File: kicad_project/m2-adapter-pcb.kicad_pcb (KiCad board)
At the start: 2 copper layers, 100 x 45 mm, 19 parts, among them J1 Bus_M.2_Socket_B, J2 SATA-7P, J3 JST S2B-PH-K-S, U1 TPS563200

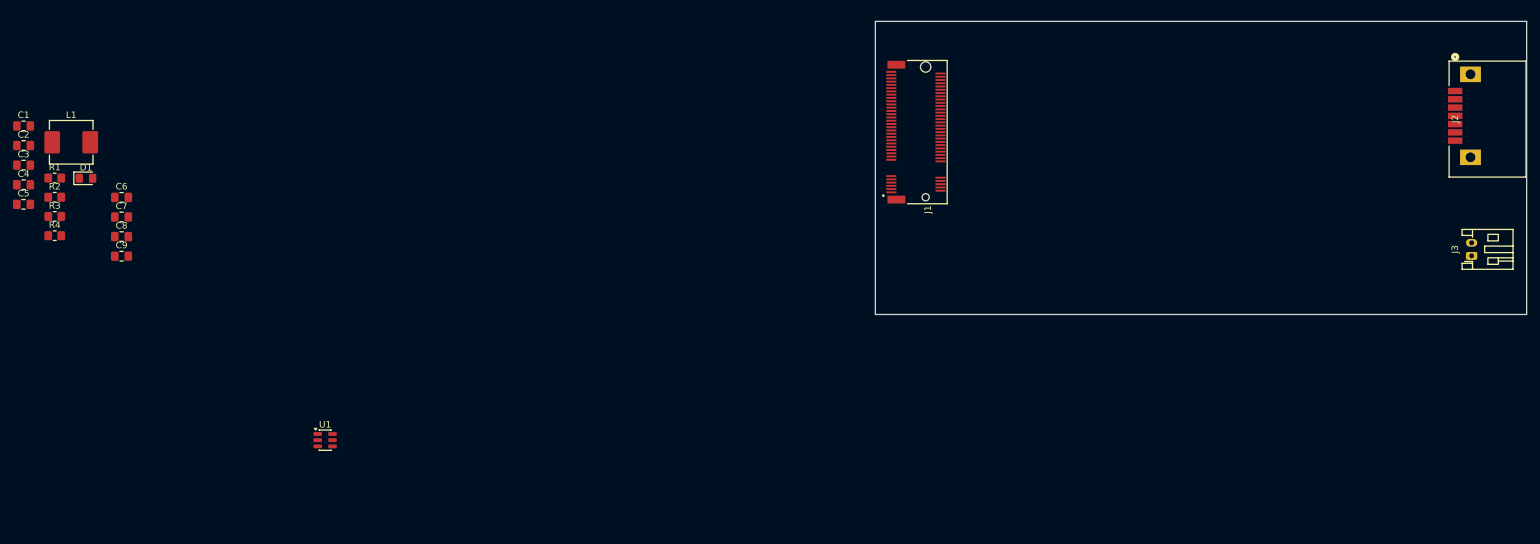
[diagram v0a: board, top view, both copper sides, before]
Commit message: Update buck converter schematics
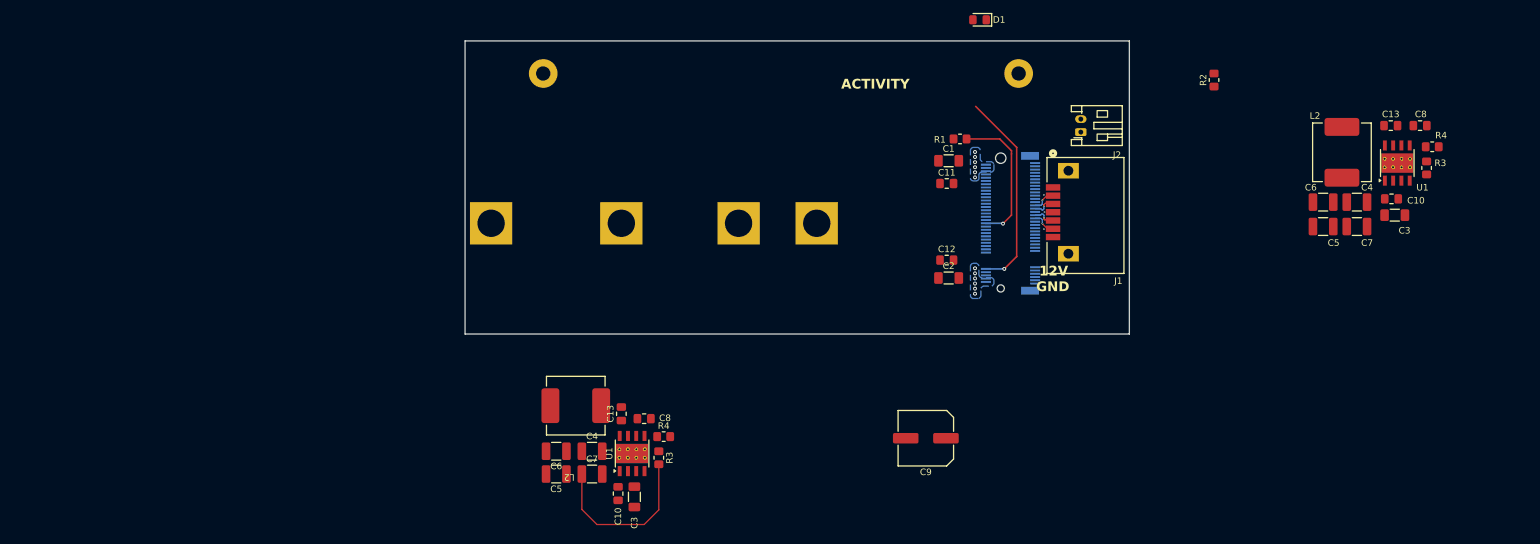
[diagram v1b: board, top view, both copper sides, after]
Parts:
- removed the C3 at (28.2, 66.1)
- removed the C4 at (28.2, 69.1)
- removed the C5 at (28.2, 72.1)
- removed L1: 3.3uH, Inductor_SMD:L_Vishay_IHLP-2525
- removed the R3 at (33.0, 74.0)
- removed the R4 at (33.0, 76.9)
- removed the U1 at (74.5, 108.3)
- added C10: 0.22uF, Capacitor_SMD:C_0805_2012Metric_Pad1.18x1.45mm_HandSolder, F.Cu at (119.5, 116.5)
- added C10: 0.22uF, Capacitor_SMD:C_0805_2012Metric_Pad1.18x1.45mm_HandSolder, F.Cu at (238.2, 71.2)
- added C11: 0.1uF, Capacitor_SMD:C_0805_2012Metric_Pad1.18x1.45mm_HandSolder, F.Cu at (170.0, 68.9)
- added C12: 0.1uF, Capacitor_SMD:C_0805_2012Metric_Pad1.18x1.45mm_HandSolder, F.Cu at (170.0, 80.7)
- added C13: 0.1uF, Capacitor_SMD:C_0805_2012Metric_Pad1.18x1.45mm_HandSolder, F.Cu at (238.1, 60.0)
- added C13: 0.1uF, Capacitor_SMD:C_0805_2012Metric_Pad1.18x1.45mm_HandSolder, F.Cu at (120.0, 104.2)
- added C3: 10uF, Capacitor_SMD:C_1206_3216Metric_Pad1.33x1.80mm_HandSolder, F.Cu at (238.8, 73.8)
- added C3: 10uF, Capacitor_SMD:C_1206_3216Metric_Pad1.33x1.80mm_HandSolder, F.Cu at (122.0, 117.0)
- added C4: 22uF, Capacitor_SMD:C_1210_3225Metric_Pad1.33x2.70mm_HandSolder, F.Cu at (115.5, 110.0)
- added C4: 22uF, Capacitor_SMD:C_1210_3225Metric_Pad1.33x2.70mm_HandSolder, F.Cu at (232.9, 71.8)
- added C5: 22uF, Capacitor_SMD:C_1210_3225Metric_Pad1.33x2.70mm_HandSolder, F.Cu at (227.8, 75.5)
- added C5: 22uF, Capacitor_SMD:C_1210_3225Metric_Pad1.33x2.70mm_HandSolder, F.Cu at (110.0, 113.5)
- added C6: 22uF, Capacitor_SMD:C_1210_3225Metric_Pad1.33x2.70mm_HandSolder, F.Cu at (227.8, 71.8)
- added C7: 22uF, Capacitor_SMD:C_1210_3225Metric_Pad1.33x2.70mm_HandSolder, F.Cu at (232.9, 75.5)
- added C8: 1uF, Capacitor_SMD:C_0805_2012Metric_Pad1.18x1.45mm_HandSolder, F.Cu at (242.6, 60.0)
- added H1: MountingHole_Pad, m2-adapter-pcb:M.2_Standoff_Hole, B.Cu at (100.0, 75.0)
- added H2: MountingHole_Pad, m2-adapter-pcb:M.2_Standoff_Hole, B.Cu at (150.0, 75.0)
- added H3: MountingHole_Pad, m2-adapter-pcb:M.2_Standoff_Hole, B.Cu at (138.0, 75.0)
- added H4: MountingHole_Pad, m2-adapter-pcb:M.2_Standoff_Hole, B.Cu at (120.0, 75.0)
- added H5: MountingHole_Pad, MountingHole:MountingHole_2.2mm_M2_Pad, F.Cu at (108.0, 52.0)
- added H6: MountingHole_Pad, MountingHole:MountingHole_2.2mm_M2_Pad, F.Cu at (181.0, 52.0)
- added L2: 6.8uH, m2-adapter-pcb:L_MPX1D0840, F.Cu at (113.0, 103.0)
- added L2: 6.8uH, m2-adapter-pcb:L_MPX1D0840, F.Cu at (230.6, 64.1)
- added R3: 100kOhm, Resistor_SMD:R_0805_2012Metric_Pad1.20x1.40mm_HandSolder, F.Cu at (125.8, 111.0)
- added R3: 100kOhm, Resistor_SMD:R_0805_2012Metric_Pad1.20x1.40mm_HandSolder, F.Cu at (243.6, 66.5)
- added R4: 43kOhm, Resistor_SMD:R_0805_2012Metric_Pad1.20x1.40mm_HandSolder, F.Cu at (244.5, 63.2)
- added R4: 43kOhm, Resistor_SMD:R_0805_2012Metric_Pad1.20x1.40mm_HandSolder, F.Cu at (126.5, 107.8)
- added U1: LMR33630ADDA, Package_SO:Texas_HSOP-8-1EP_3.9x4.9mm_P1.27mm_ThermalVias, F.Cu at (239.1, 65.8)
- added U1: LMR33630ADDA, Package_SO:Texas_HSOP-8-1EP_3.9x4.9mm_P1.27mm_ThermalVias, F.Cu at (121.7, 110.3)
- C1, C2: footprint Capacitor_SMD:C_0805_2012Metric_Pad1.18x1.45mm_HandSolder -> Capacitor_SMD:C_1206_3216Metric_Pad1.33x1.80mm_HandSolder
- C6, C7: value 10uF -> 22uF; footprint Capacitor_SMD:C_0805_2012Metric_Pad1.18x1.45mm_HandSolder -> Capacitor_SMD:C_1210_3225Metric_Pad1.33x2.70mm_HandSolder
- C8: value 0.1uF -> 1uF
- C9: value 0.1uF -> 100uF; footprint Capacitor_SMD:C_0805_2012Metric_Pad1.18x1.45mm_HandSolder -> Capacitor_SMD:C_Elec_8x6.2
- J3: renamed from J1; moved to B.Cu
- moved R2 178.9 mm to (211.0, 53.0), turned to 90 degrees
- moved C2 143.5 mm to (170.2, 83.4)
- moved C1 142.1 mm to (170.2, 65.4)
- moved D1 139.3 mm to (175.0, 43.8), turned to 180 degrees
- moved R1 139.1 mm to (172.0, 62.0), turned to 180 degrees
- moved C9 126.6 mm to (166.8, 108.0), turned to 180 degrees
- moved C8 85.0 mm to (123.5, 105.0)
- moved C7 82.3 mm to (115.5, 113.5)
- moved C6 77.3 mm to (110.0, 110.0), turned to 180 degrees
- moved J1 63.5 mm to (191.3, 73.8)
- moved J2 62.9 mm to (190.6, 61.0)
- moved J3 18.1 mm to (178.2, 75.0)
- renumbered J2 to J1, J3 to J2
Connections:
- net Net-(J1-PERn0/SATA-B+) renamed SATA_B+
- net Net-(J1-PERp0/SATA-B-) renamed SATA_B-
- net Net-(J1-PETn0/SATA-A-) renamed SATA_A-
- net Net-(J1-PETp0/SATA-A+) renamed SATA_A+
- C1 pad 1: Net-(J3-Pin_2) -> +3.3V
- C2 pad 1: Net-(J3-Pin_2) -> +3.3V
- C8 pad 1: +3.3V -> Net-(U1-VCC)
- C9 pad 1: +3.3V -> VIN
- J2 pad 2: Net-(J3-Pin_2) -> VIN
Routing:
- net Net-(D1-K): track 0.00 -> 31.2 mm, vias 0 -> 1
- net +3.3V: track 0.00 -> 26.1 mm, vias 0 -> 12
- net Net-(J3-DEVSLP): track 0.00 -> 22.1 mm, vias 0 -> 1
- net SATA_A+: track 0.00 -> 3.75 mm, vias 0 -> 1
- net SATA_B+: track 0.00 -> 3.72 mm, vias 0 -> 1
- net SATA_A-: track 0.00 -> 3.64 mm, vias 0 -> 1
- net SATA_B-: track 0.00 -> 3.53 mm, vias 0 -> 1
- net GND: vias 0 -> 3
- added copper zone on B.Cu, net +3.3V
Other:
- board size 100 x 45 mm -> 102 x 45 mm
- board text added: "12V"
- board text added: "ACTIVITY"
- board text added: "GND"

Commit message: Finish routing
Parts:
- removed the C10 at (119.5, 116.5)
- removed the C10 at (238.2, 71.2)
- removed the C13 at (238.1, 60.0)
- removed the C13 at (120.0, 104.2)
- removed the C3 at (238.8, 73.8)
- removed the C3 at (122.0, 117.0)
- removed the C4 at (115.5, 110.0)
- removed the C4 at (232.9, 71.8)
- removed the C5 at (227.8, 75.5)
- removed the C5 at (110.0, 113.5)
- removed the C6 at (227.8, 71.8)
- removed the C6 at (110.0, 110.0)
- removed the C7 at (232.9, 75.5)
- removed the C7 at (115.5, 113.5)
- removed the C8 at (242.6, 60.0)
- removed the C8 at (123.5, 105.0)
- removed the L2 at (113.0, 103.0)
- removed the L2 at (230.6, 64.1)
- removed the R3 at (125.8, 111.0)
- removed the R3 at (243.6, 66.5)
- removed the R4 at (244.5, 63.2)
- removed the R4 at (126.5, 107.8)
- removed the U1 at (239.1, 65.8)
- removed the U1 at (121.7, 110.3)
- added C10: 0.22uF, Capacitor_SMD:C_0805_2012Metric_Pad1.18x1.45mm_HandSolder, F.Cu at (158.9, 58.7)
- added C13: 0.1uF, Capacitor_SMD:C_0805_2012Metric_Pad1.18x1.45mm_HandSolder, F.Cu at (148.0, 59.4)
- added C3: 10uF, Capacitor_SMD:C_1206_3216Metric_Pad1.33x1.80mm_HandSolder, F.Cu at (161.4, 58.5)
- added C4: 22uF, Capacitor_SMD:C_1210_3225Metric_Pad1.33x2.70mm_HandSolder, F.Cu at (161.7, 64.1)
- added C5: 22uF, Capacitor_SMD:C_1210_3225Metric_Pad1.33x2.70mm_HandSolder, F.Cu at (169.1, 64.1)
- added C6: 22uF, Capacitor_SMD:C_1210_3225Metric_Pad1.33x2.70mm_HandSolder, F.Cu at (172.6, 64.1)
- added C7: 22uF, Capacitor_SMD:C_1210_3225Metric_Pad1.33x2.70mm_HandSolder, F.Cu at (165.5, 64.1)
- added C8: 1uF, Capacitor_SMD:C_0805_2012Metric_Pad1.18x1.45mm_HandSolder, F.Cu at (147.1, 55.8)
- added L2: 6.8uH, m2-adapter-pcb:L_MPX1D0840, F.Cu at (153.9, 65.5)
- added R3: 100kOhm, Resistor_SMD:R_0805_2012Metric_Pad1.20x1.40mm_HandSolder, F.Cu at (154.1, 53.0)
- added R4: 43kOhm, Resistor_SMD:R_0805_2012Metric_Pad1.20x1.40mm_HandSolder, F.Cu at (149.9, 53.0)
- added U1: LMR33630ADDA, Package_SO:Texas_HSOP-8-1EP_3.9x4.9mm_P1.27mm_ThermalVias, F.Cu at (153.5, 57.6)
- J1: footprint m2-adapter-pcb:CONN_67490-1220_MOL -> m2-adapter-pcb:AMPHENOL_SAT3M2132072TR
- moved R2 80.4 mm to (130.8, 58.2)
- moved C9 51.8 mm to (168.7, 56.2), turned to 0 degrees
- moved D1 46.3 mm to (129.8, 53.5), turned to 0 degrees
- moved R1 13.0 mm to (170.7, 75.0)
- moved C1 11.0 mm to (180.5, 69.5)
- moved C12 10.8 mm to (180.5, 83.0)
- moved C11 10.6 mm to (180.5, 67.2)
- moved C2 10.6 mm to (180.5, 80.8)
- moved J2 2.10 mm to (191.2, 59.0)
- moved J1 1.97 mm to (189.3, 73.8)
- moved H1 0.72 mm to (100.7, 75.0)
- moved H2 0.72 mm to (150.7, 75.0)
- moved H3 0.72 mm to (138.7, 75.0)
- moved H4 0.72 mm to (120.7, 75.0)
- moved J3 0.72 mm to (179.0, 75.0)
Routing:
- net +3.3V: track 26.1 -> 92.8 mm, vias 12 -> 10
- net Net-(D1-K): track 31.2 -> 73.7 mm
- net Net-(J3-DEVSLP): track 22.1 -> 4.97 mm
- net Net-(U1-FB): track 0.00 -> 4.98 mm
- net Net-(D1-A): track 0.00 -> 3.76 mm
- net Net-(U1-VCC): track 0.00 -> 3.17 mm
- net Net-(U1-BOOT): track 0.00 -> 2.82 mm
- net SATA_B+: track 3.72 -> 2.61 mm
- net SATA_A+: track 3.75 -> 2.71 mm
- net SATA_A-: track 3.64 -> 2.61 mm
- net SATA_B-: track 3.53 -> 2.60 mm
- net GND: vias 3 -> 30
- added copper zone on F.Cu, net +3.3V
- added copper zone on B.Cu, net GND
- added copper zone on F.Cu, net GND
- added copper zone on F.Cu, net SW
- added copper zone on F.Cu, net VIN
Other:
- board size 102 x 45 mm -> 102 x 43 mm
- board text added: "(c) 2025 - Sergio Carmine"
- board text added: "2230"
- board text added: "2242"
- board text added: "2260"
- board text added: "2280"
- board text added: "M.2 to SATA adapter PCB"
- board text added: "SATA M.2"
